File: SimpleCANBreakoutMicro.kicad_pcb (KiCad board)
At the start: 2 copper layers, 20 x 15 mm, 12 parts, among them J1 Conn_01x04_Pin, J2 Conn_01x04_Pin, U2 XC6206PxxxMR, U3 SN65HVD230

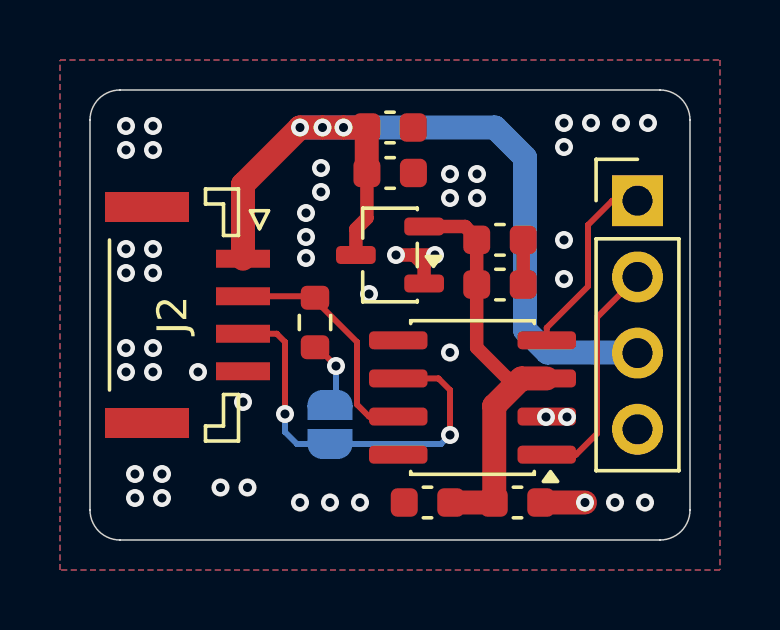
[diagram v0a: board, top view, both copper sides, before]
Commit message: Add bottom pads, silkscreen
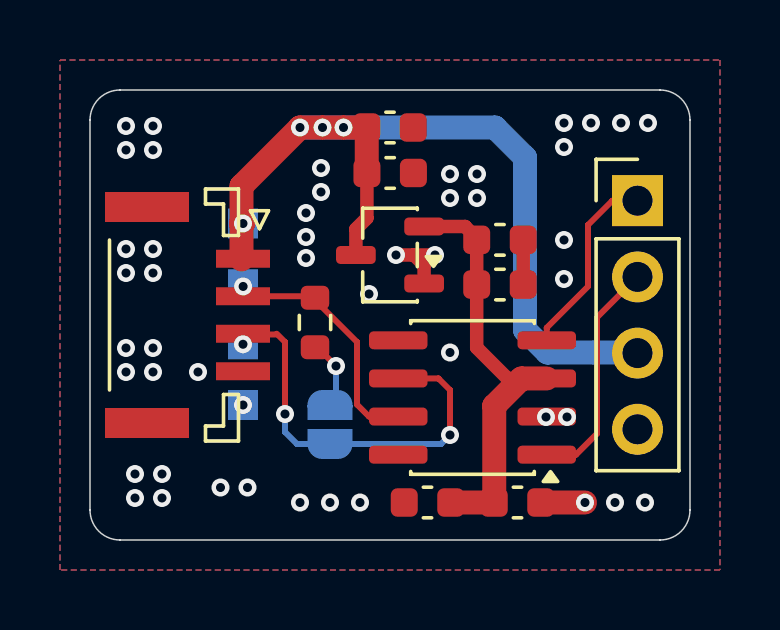
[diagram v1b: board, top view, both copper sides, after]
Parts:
- added TP1: TestPoint, TestPoint:TestPoint_Pad_1.0x1.0mm, B.Cu at (131.1, 61.5)
- added TP2: TestPoint, TestPoint:TestPoint_Pad_1.0x1.0mm, B.Cu at (131.1, 63.5)
- added TP3: TestPoint, TestPoint:TestPoint_Pad_1.0x1.0mm, B.Cu at (131.1, 65.5)
- added TP4: TestPoint, TestPoint:TestPoint_Pad_1.0x1.0mm, B.Cu at (131.1, 67.5)
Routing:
- net /CANL: track 13.7 -> 13.9 mm, vias 2 -> 3
- net +5V: track 29.7 -> 29.8 mm, vias 3 -> 4
- net /CANH: track 8.10 -> 8.23 mm, vias 0 -> 1
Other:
- board text added: "120"
- board text added: "5"
- board text added: "G"
- board text added: "H"
- board text added: "L"
